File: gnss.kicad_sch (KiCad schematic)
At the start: 76 parts, among them J3 Conn_Coaxial, J4 Conn_Coaxial_Small, Q2 AO3401A, Q5 BSS138, SW1 SW_Push, SW2 SW_Push, U11 TPS7A2033PDBVR, U2 NEO-M9N, U8 TPS259474LRPWR

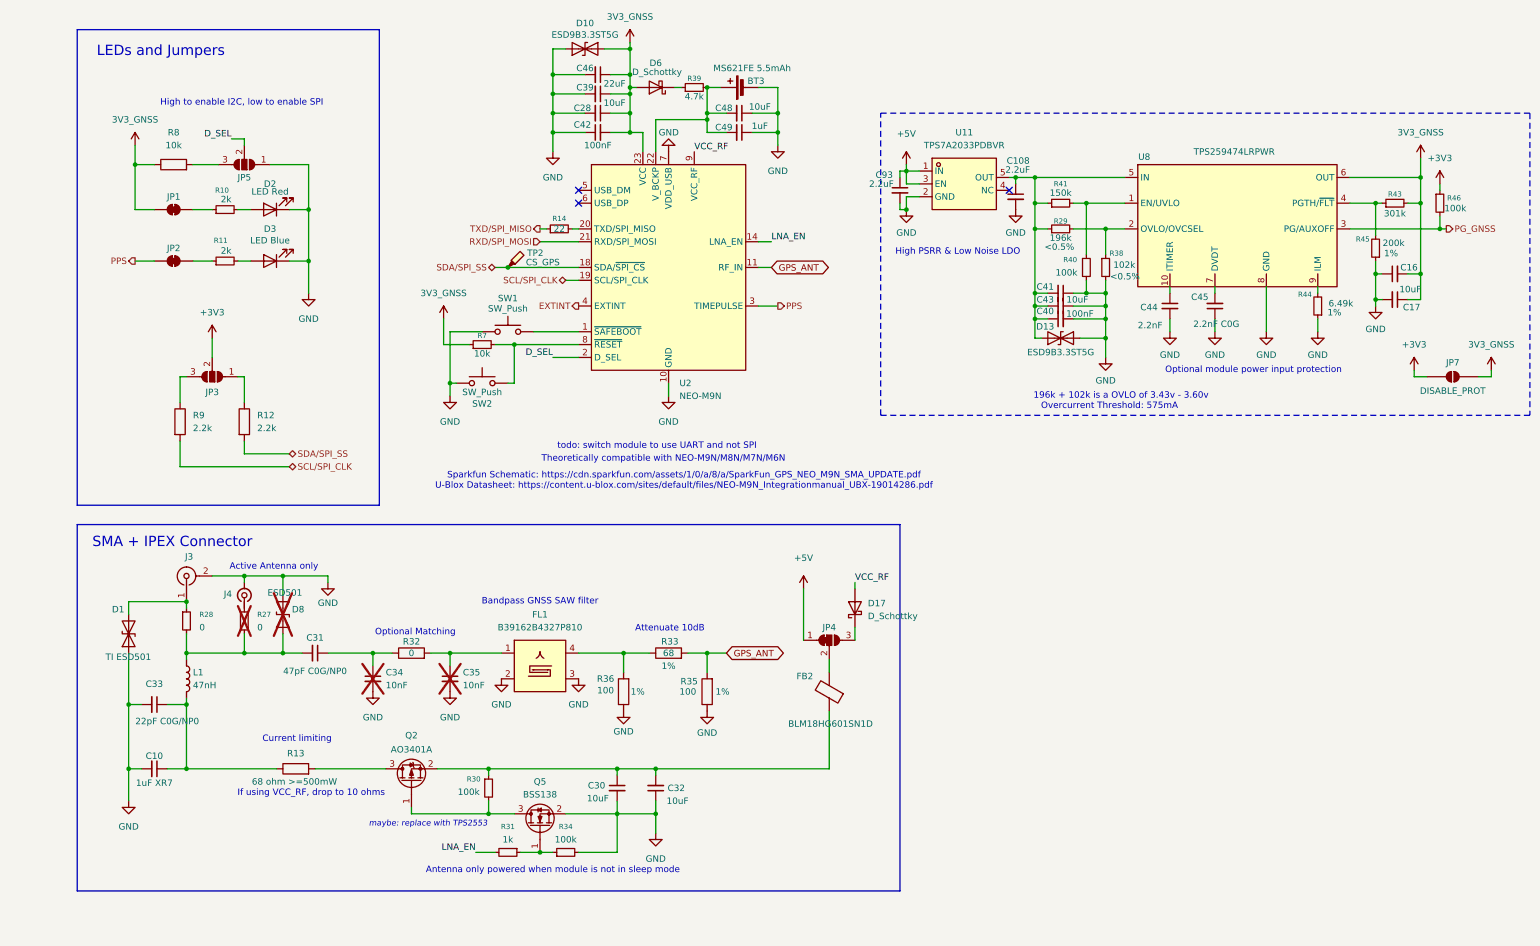
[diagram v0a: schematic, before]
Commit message: rename sheets, add lora antenna detect, seperate charger and regulator schematics, add eFuse to 5v output
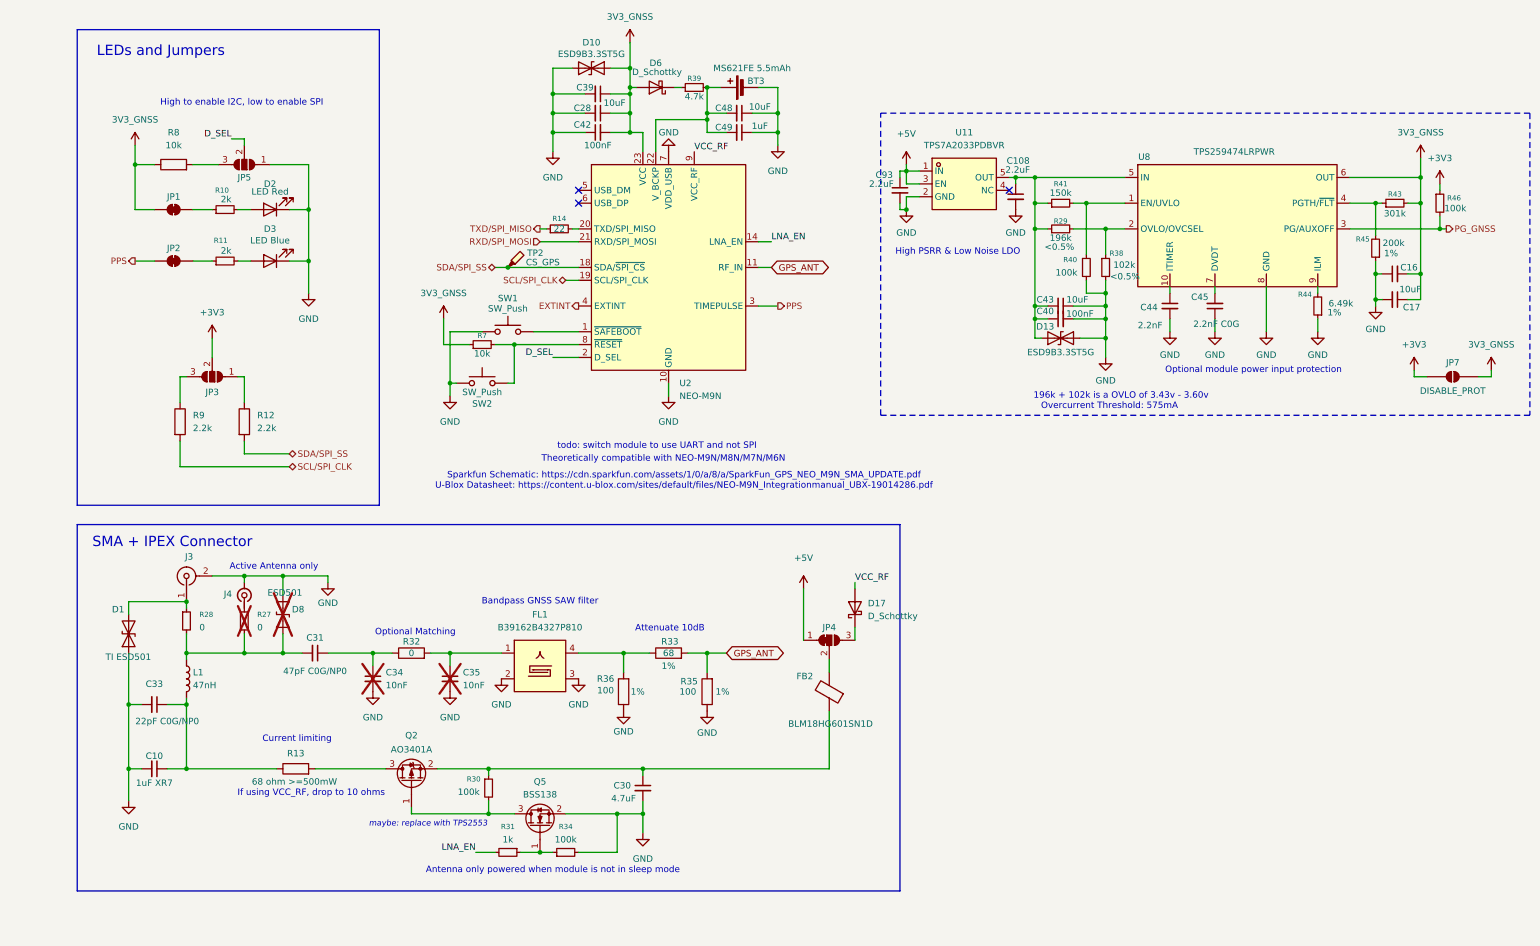
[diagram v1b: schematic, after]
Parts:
- removed C32, C41: 10uF, Capacitor_SMD:C_0603_1608Metric, symbol Device:C_Small
- removed C46: 22uF, Capacitor_SMD:C_0805_2012Metric, symbol Device:C_Small
- C30: value 10uF -> 4.7uF
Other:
- moved on the sheet: C30, D10

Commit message: Reworking power rails, adding antenna detection, and organization
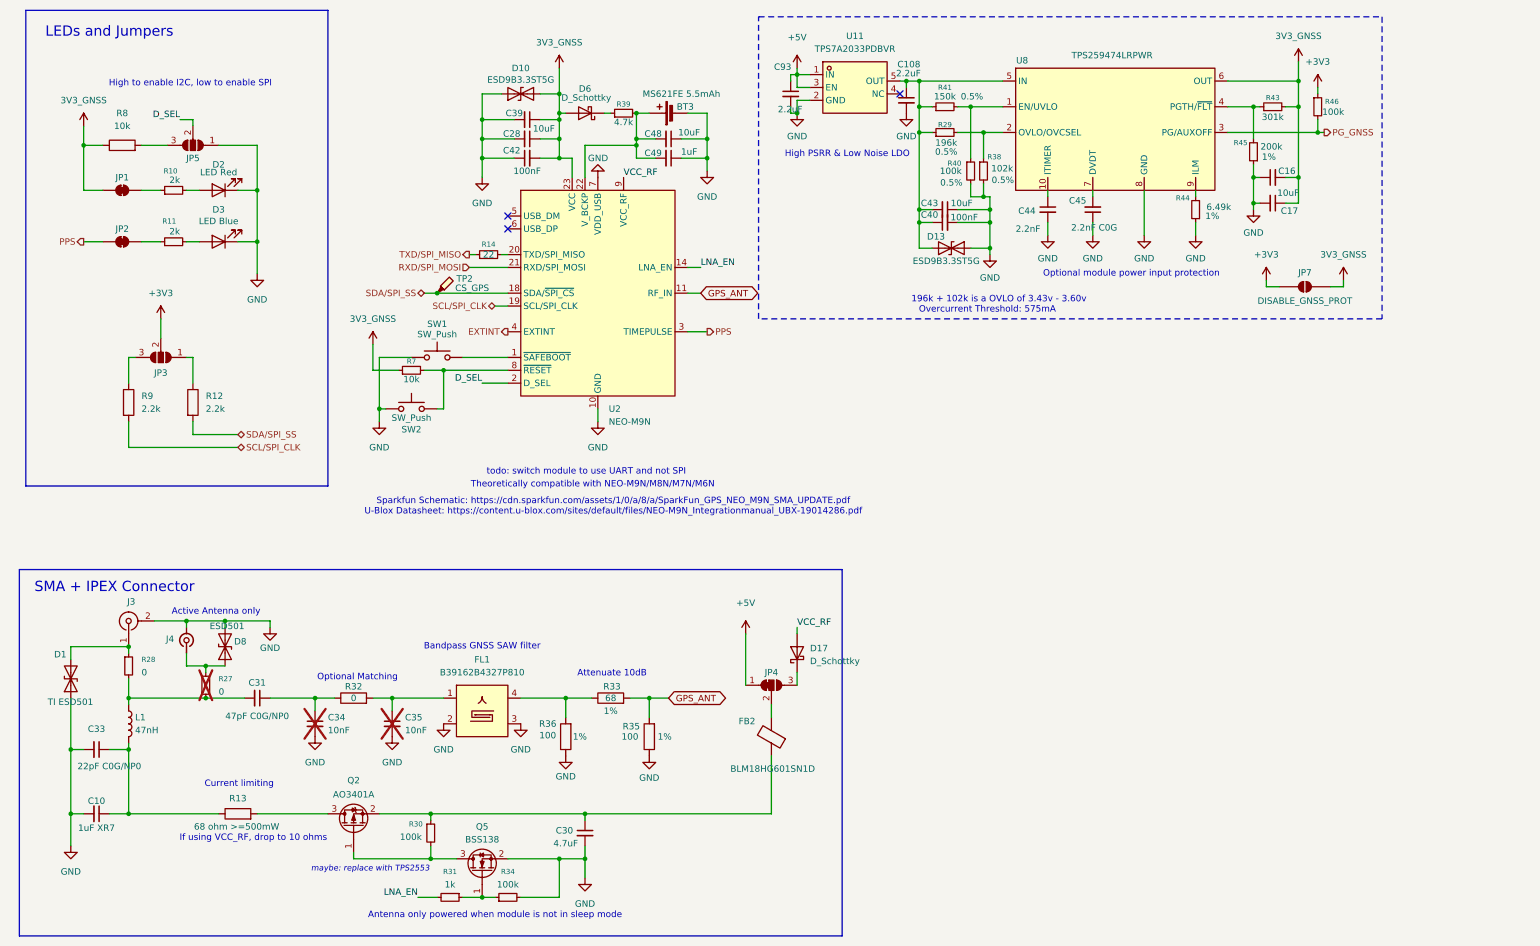
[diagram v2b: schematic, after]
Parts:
- D8: now fitted
- JP7: value DISABLE_PROT -> DISABLE_GNSS_PROT
- R29, R38: Tolerance <0.5% -> 0.5%
- R40, R41: Tolerance (none) -> 0.5%
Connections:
- net at J4.1 (In), R27.1: now also D8.1 (A1)
- net at C31.2, L1.1, R27.2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: no longer D8.1 (A1)
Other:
- moved on the sheet: BT3, C10, C108, C16, C17, C28, C30, C31, C33, C34, C35, C39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

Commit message: push to work on laptop2
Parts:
- removed D10, D13: ESD9B3.3ST5G, Diode_SMD:D_SOD-923, symbol Diode:ESD9B3.3ST5G
- added D11: ESD351DPYR, Diode_SMD:D_0402_1005Metric, symbol Device:D_TVS
- added D13: TPD1E10B06, Package_SON:Texas_DPY0002A_0.6x1mm_P0.65mm, symbol Diode:ESD9B5.0ST5G
- D6: value D_Schottky -> RB531SM-30; footprint (none) -> Diode_SMD:D_SOD-523; LCSC Part (none) -> C2766159
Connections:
- net 3V3_GNSS: now also D11.1 (A1)
- net GND: now also D11.2 (A2), D13.2 (A2)
- net at C108.1, C40.1, C43.2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: now also D13.1 (A1)
- net SDA/SPI_SS renamed SDA/SPI_CS
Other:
- company: (none) -> Ryan Di Lorenzo
- title: (none) -> GNSS Module / Active RF Antenna

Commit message: push for review, minor changes
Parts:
- removed JP5: SolderJumper_3_Open, Jumper:SolderJumper-3_P1.3mm_Open_RoundedPad1.0x1.5mm_NumberLabels, symbol Jumper:SolderJumper_3_Open
- added JP10: I2C/UART/SPI, Jumper:SolderJumper-3_P1.3mm_Open_RoundedPad1.0x1.5mm_NumberLabels, symbol Jumper:SolderJumper_3_Bridged12
- renumbered C33 to C79, C10 to C80, C31 to C81, C34 to C82, C35 to C83, C39 to C84, C28 to C85, C42 to C86, C30 to C87, C48 to C88, C49 to C89, C93 to C90, C108 to C91, C43 to C92, C40 to C93, C44 to C94, C45 to C95, C16 to C96, C17 to C97, D11 to D10, D6 to D11, D17 to D12, D1 to D6, D2 to D7, D3 to D8, D8 to D9, FB2 to FB1, J3 to J7, J4 to J8, JP4 to JP11, JP7 to JP12, JP1 to JP7, JP2 to JP8, JP3 to JP9, L1 to L2, Q2 to Q8, Q5 to Q9, R8 to R47, R9 to R48, R28 to R49, R10 to R50, R11 to R51, R12 to R52, R27 to R53, R13 to R54, R32 to R55, R7 to R56, R30 to R57, R31 to R58, R14 to R59, R34 to R60, R36 to R61, R33 to R62, R39 to R63, R35 to R64, R41 to R65, R29 to R66, R40 to R67, R38 to R68, R44 to R69, R45 to R70, R43 to R71, R46 to R72, SW2 to SW4, SW1 to SW5, TP2 to TP5, U8 to U10, U2 to U8, U11 to U9
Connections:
- net D_SEL: now also JP10.2 (C)
- net GND: now also JP10.3 (B)
- net at R47.2: now also JP10.1 (A)
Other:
- note added: "High to enable I2C/UART, low to enable SPI"
- note removed: "High to enable I2C, low to enable SPI"

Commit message: e-ink
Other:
- moved on the sheet: BT3, C84, C85, C86, C88, C89, D10, D11, R56, R59, R63, SW4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

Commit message: journal update!
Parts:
- removed R59: 22, Resistor_SMD:R_0402_1005Metric, symbol Device:R_Small
- C79: value 22pF C0G/NP0 -> 22pF; Capacitor Rating (none) -> C0G/NP0
- C80: value 1uF XR7 -> 1uF; Capacitor Rating (none) -> X7R
- C86, C93: Capacitor Rating (none) -> X7R; LCSC Part (none) -> C5142567; Voltage Rating (none) -> 50V
- R66: value 196k -> 215k; Tolerance 0.5% -> 0.1%
- R68: value 102k -> 113k; Tolerance 0.5% -> 0.1%
- R69: value 6.49k -> 6.65k
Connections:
- net TXD/SPI_MISO: now also U8.20 (TXD/SPI_MISO)
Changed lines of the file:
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@@
 	(wire
 		(pts
-			(xy 101.6 62.23) (xy 102.87 62.23)
+			(xy 101.6 62.23) (xy 109.22 62.23)
 		)
 		(stroke
@@
 	(wire
 		(pts
-			(xy 101.6 64.77) (xy 109.22 64.77)
-		)
-		(stroke
-			(width 0)
-			(type default)
-		)
-	)
-	(wire
-		(pts
 			(xy 191.77 27.94) (xy 208.28 27.94)
 		)
@@
 	(wire
 		(pts
+			(xy 101.6 64.77) (xy 109.22 64.77)
+		)
+		(stroke
+			(width 0)
+			(type default)
+		)
+	)
+	(wire
+		(pts
 			(xy 167.64 137.16) (xy 167.64 135.89)
 		)
@@
 	(wire
 		(pts
-			(xy 107.95 62.23) (xy 109.22 62.23)
-		)
-		(stroke
-			(width 0)
-			(type default)
-		)
-	)
-	(wire
-		(pts
 			(xy 95.25 172.72) (xy 95.25 173.99)
 		)
@@
 			)
 		)
-		(property "Value" "102k"
+		(property "Value" "113k"
 			(at 205.994 45.212 0)
 			(show_name no)
@@
 			)
 		)
-		(property "Tolerance" "0.5%"
+		(property "Tolerance" "0.1%"
 			(at 208.28 47.498 0)
 			(show_name no)
@@
 			)
 		)
+		(property "Capacitor Rating" ""
+			(at 204.47 45.72 0)
+			(hide yes)
+			(show_name no)
+			(do_not_autoplace no)
+			(effects
+				(font
+					(size 1.27 1.27)
+				)
+			)
+		)
 		(pin "1"
 		)
@@
 			)
 		)
-		(property "LCSC Part" ""
+		(property "LCSC Part" "C5142567"
 			(at 113.03 43.18 0)
 			(hide yes)
@@
 			)
 		)
-		(property "Voltage Rating" ""
+		(property "Voltage Rating" "50V"
 			(at 113.03 43.18 0)
 			(show_name no)
@@
 			)
 		)
+		(property "Capacitor Rating" "X7R"
+			(at 113.03 43.18 90)
+			(hide yes)
+			(show_name no)
+			(do_not_autoplace no)
+			(effects
+				(font
+					(size 1.27 1.27)
+				)
+			)
+		)
 		(pin "1"
 		)
@@
 			)
 		)
-		(property "Value" "196k"
+		(property "Value" "215k"
 			(at 197.104 40.132 90)
 			(show_name no)
@@
 			)
 		)
-		(property "Tolerance" "0.5%"
+		(property "Tolerance" "0.1%"
 			(at 197.104 41.91 90)
 			(show_name no)
@@
 			)
 		)
+		(property "Capacitor Rating" ""
+			(at 196.85 38.1 0)
+			(hide yes)
+			(show_name no)
+			(do_not_autoplace no)
+			(effects
+				(font
+					(size 1.27 1.27)
+				)
+			)
+		)
 		(pin "2"
 		)
@@
 	)
 	(symbol
-		(lib_id "Device:R_Small")
-		(at 105.41 62.23 90)
-		(unit 1)
-		(body_style 1)
-		(exclude_from_sim no)
-		(in_bom yes)
-		(on_board yes)
-		(in_pos_files yes)
-		(dnp no)
-		(property "Reference" "R59"
-			(at 105.41 60.198 90)
-			(show_name no)
-			(do_not_autoplace no)
-			(effects
-				(font
-					(size 1.016 1.016)
-				)
-			)
-		)
-		(property "Value" "22"
-			(at 105.41 62.23 90)
-			(show_name no)
-			(do_not_autoplace no)
-			(effects
-				(font
-					(size 1.27 1.27)
-				)
-			)
-		)
-		(property "Footprint" "Resistor_SMD:R_0402_1005Metric"
-			(at 105.41 62.23 0)
-			(hide yes)
-			(show_name no)
-			(do_not_autoplace no)
-			(effects
-				(font
-					(size 1.27 1.27)
-				)
-			)
-		)
-		(property "Datasheet" ""
-			(at 105.41 62.23 0)
-			(hide yes)
-			(show_name no)
-			(do_not_autoplace no)
-			(effects
-				(font
-					(size 1.27 1.27)
-				)
-			)
-		)
-		(property "Description" "Resistor, small symbol"
-			(at 105.41 62.23 0)
-			(hide yes)
-			(show_name no)
-			(do_not_autoplace no)
-			(effects
-				(font
-					(size 1.27 1.27)
-				)
-			)
-		)
-		(property "LCSC Part" ""
-			(at 105.41 62.23 0)
-			(hide yes)
-			(show_name no)
-			(do_not_autoplace no)
-			(effects
-				(font
-					(size 1.27 1.27)
-				)
-			)
-		)
-		(property "Voltage Rating" ""
-			(at 105.41 62.23 0)
-			(hide yes)
-			(show_name no)
-			(do_not_autoplace no)
-			(effects
-				(font
-					(size 1.27 1.27)
-				)
-			)
-		)
-		(property "Tolerance" ""
-			(at 105.41 62.23 0)
-			(hide yes)
-			(show_name no)
-			(do_not_autoplace no)
-			(effects
-				(font
-					(size 1.27 1.27)
-				)
-			)
-		)
-		(property "LCSC" ""
-			(at 105.41 62.23 90)
-			(hide yes)
-			(show_name no)
-			(do_not_autoplace no)
-			(effects
-				(font
-					(size 1.27 1.27)
-				)
-			)
-		)
-		(property "KLC_S3.3" ""
-			(at 105.41 62.23 90)
-			(hide yes)
-			(show_name no)
-			(do_not_autoplace no)
-			(effects
-				(font
-					(size 1.27 1.27)
-				)
-			)
-		)
-		(property "KLC_S5.1" ""
-			(at 105.41 62.23 90)
-			(hide yes)
-			(show_name no)
-			(do_not_autoplace no)
-			(effects
-				(font
-					(size 1.27 1.27)
-				)
-			)
-		)
-		(pin "2"
-		)
-		(pin "1"
-		)
-		(instances
-			(project "parsnip"
-				(path "/fe9d4a31-2311-442f-997c-52ad8ca5cfe9/5443eb24-9bcb-4330-89ee-947146bd4a27"
-					(reference "R59")
-					(unit 1)
-				)
-			)
-		)
-	)
-	(symbol
 		(lib_id "Device:C_Small")
 		(at 60.96 149.86 270)
@@
 			)
 		)
-		(property "LCSC Part" ""
+		(property "LCSC Part" "C5142567"
 			(at 196.85 55.88 0)
 			(hide yes)
@@
 			)
 		)
-		(property "Voltage Rating" ""
+		(property "Voltage Rating" "50V"
 			(at 196.85 55.88 0)
 			(show_name no)
@@
 			)
 		)
+		(property "Capacitor Rating" "X7R"
+			(at 196.85 55.88 90)
+			(hide yes)
+			(show_name no)
+			(do_not_autoplace no)
+			(effects
+				(font
+					(size 1.27 1.27)
+				)
+			)
+		)
 		(pin "1"
 		)
@@
 			)
 		)
-		(property "Value" "6.49k"
+		(property "Value" "6.65k"
 			(at 250.952 52.832 0)
 			(show_name no)
@@
 			)
 		)
+		(property "Capacitor Rating" ""
+			(at 246.38 53.34 0)
+			(hide yes)
+			(show_name no)
+			(do_not_autoplace no)
+			(effects
+				(font
+					(size 1.27 1.27)
+				)
+			)
+		)
 		(pin "2"
 		)
@@
 			)
 		)
-		(property "Value" "22pF C0G/NP0"
-			(at 31.75 163.322 90)
+		(property "Value" "22pF"
+			(at 32.512 158.496 90)
 			(show_name no)
 			(do_not_autoplace no)
@@
 			)
 		)
+		(property "Capacitor Rating" "C0G/NP0"
+			(at 29.464 162.814 90)
+			(show_name no)
+			(do_not_autoplace no)
+			(effects
+				(font
+					(size 1.27 1.27)
+				)
+			)
+		)
 		(pin "2"
 		)
@@
 			)
 		)
-		(property "Value" "1uF XR7"
+		(property "Value" "1uF"
 			(at 29.21 175.514 90)
 			(show_name no)
@@
 			(hide yes)
 			(show_name no)
+			(do_not_autoplace no)
+			(effects
+				(font
+					(size 1.27 1.27)
+				)
+			)
+		)
+		(property "Capacitor Rating" "X7R"
+			(at 29.21 172.72 0)
+			(hide yes)
+			(show_name no)

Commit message: pcb layout!
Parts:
- C100: renamed from C86; LCSC Part C5142567 -> C5272680
- C101: renamed from C87; LCSC Part (none) -> C6119795
- C102: renamed from C88; LCSC Part (none) -> C6119763
- C103: renamed from C89; LCSC Part (none) -> C7472948
- C104: renamed from C90; footprint (none) -> Capacitor_SMD:C_0402_1005Metric; LCSC Part (none) -> C33546001
- C105: renamed from C91; footprint (none) -> Capacitor_SMD:C_0402_1005Metric; LCSC Part (none) -> C33546001
- C106: renamed from C92; LCSC Part (none) -> C6119763
- C107: renamed from C93; LCSC Part C5142567 -> C5272680
- C108: renamed from C94; footprint (none) -> Capacitor_SMD:C_0402_1005Metric; LCSC Part (none) -> C2987940
- C109: renamed from C95; value 2.2nF C0G -> 2.2nF; Capacitor Rating (none) -> C0G; LCSC Part (none) -> C2987940
- C110: renamed from C96; LCSC Part (none) -> C7393892
- C111: renamed from C97; LCSC Part (none) -> C6119763
- C93: renamed from C79; LCSC Part (none) -> C696857
- C94: renamed from C80; LCSC Part (none) -> C53426846
- C95: renamed from C81; value 47pF C0G/NP0 -> 47pF; Capacitor Rating (none) -> C0G; LCSC Part (none) -> C20069324
- C98: renamed from C84; LCSC Part (none) -> C7393892
- C99: renamed from C85; LCSC Part (none) -> C6119763
- D11: renamed from D7; footprint LED_THT:LED_D5.0mm -> LED_SMD:LED_0805_2012Metric; LCSC Part (none) -> C51933307
- D12: renamed from D8; footprint LED_THT:LED_D5.0mm -> LED_SMD:LED_0805_2012Metric; LCSC Part (none) -> C51933309
- D16: renamed from D12; value D_Schottky -> RB531SM-30T2R; footprint (none) -> Diode_SMD:D_SOD-523; LCSC Part (none) -> C2766159
- FB1: LCSC Part (none) -> C85830
- FL1: LCSC Part (none) -> C2650956
- JP13: renamed from JP12; footprint (none) -> Jumper:SolderJumper-2_P1.3mm_Open_RoundedPad1.0x1.5mm
- Q12: renamed from Q8; LCSC Part (none) -> C347476
- Q13: renamed from Q9; LCSC Part (none) -> C3015220
- R67: renamed from R47; LCSC Part (none) -> C2902636
- R68: renamed from R48; footprint Resistor_SMD:R_0603_1608Metric -> Resistor_SMD:R_0402_1005Metric_Pad0.72x0.64mm_HandSolder; LCSC Part (none) -> C23901508
- R69: renamed from R49; LCSC Part (none) -> C844711
- R70: renamed from R50; LCSC Part (none) -> C23539935
- R71: renamed from R51; value 2k -> 1k
- R72: renamed from R52; footprint Resistor_SMD:R_0603_1608Metric -> Resistor_SMD:R_0402_1005Metric_Pad0.72x0.64mm_HandSolder; LCSC Part (none) -> C23901508
- R73: renamed from R53; LCSC Part (none) -> C844711
- R74: renamed from R54; value 68 ohm >=500mW -> 62; footprint Resistor_SMD:R_1206_3216Metric_Pad1.30x1.75mm_HandSolder -> Resistor_SMD:R_0805_2012Metric; LCSC Part (none) -> C560547; Power Rating (none) -> 500mW
- R75: renamed from R55; LCSC Part (none) -> C844711
- R76: renamed from R56; LCSC Part (none) -> C2902636
- R77: renamed from R57; footprint (none) -> Resistor_SMD:R_0402_1005Metric; LCSC Part (none) -> C2984406
- R78: renamed from R58; footprint (none) -> Resistor_SMD:R_0402_1005Metric; LCSC Part (none) -> C48533754
- R79: renamed from R60; footprint (none) -> Resistor_SMD:R_0402_1005Metric; LCSC Part (none) -> C2984406
- R80: renamed from R61; value 100 -> 150; LCSC Part (none) -> C319853
- R81: renamed from R62; value 68 -> 37.4; LCSC Part (none) -> C49275310
- R82: renamed from R63; LCSC Part (none) -> C317921
- R83: renamed from R64; value 100 -> 150; LCSC Part (none) -> C319853
- R84: renamed from R65; footprint (none) -> Resistor_SMD:R_0402_1005Metric; LCSC Part (none) -> C319872
- R85: renamed from R66; LCSC Part (none) -> C861226
- R86: renamed from R67; footprint (none) -> Resistor_SMD:R_0402_1005Metric; LCSC Part (none) -> C2984406
- R87: renamed from R68; LCSC Part (none) -> C1509597
- R88: renamed from R69; LCSC Part (none) -> C47125286
- R89: renamed from R70; LCSC Part (none) -> C4354980
- R90: renamed from R71; footprint (none) -> Resistor_SMD:R_0402_1005Metric; LCSC Part (none) -> C2936623
- R91: renamed from R72; footprint (none) -> Resistor_SMD:R_0402_1005Metric; LCSC Part (none) -> C2984406
- SW4: value SW_Push -> RESET_GNSS; LCSC Part (none) -> C2681476
- SW5: value SW_Push -> SAFEBOOT_GNSS; LCSC Part (none) -> C2681476
- U9: renamed from U8; LCSC Part (none) -> C5119087
- renumbered C82 to C96, C83 to C97, D6 to D10, D9 to D13, D10 to D14, D11 to D15, D13 to D17, J7 to J11, J8 to J12, JP9 to JP10, JP10 to JP11, JP11 to JP12, JP7 to JP8, JP8 to JP9, U9 to U10, U10 to U11
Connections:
- net +3V3: no longer JP10.2 (C)
- net 3V3_GNSS: now also JP10.2 (C)
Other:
- note added: "Attenuate 6dB"
- note removed: "Attenuate 10dB"
